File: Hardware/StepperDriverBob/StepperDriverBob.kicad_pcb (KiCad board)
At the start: 2 copper layers, 43.2 x 45.7 mm, 25 parts, among them J1 CONN_01X11, P1 CONN_01X02, P2 CONN_01X04, U1 DRV8825

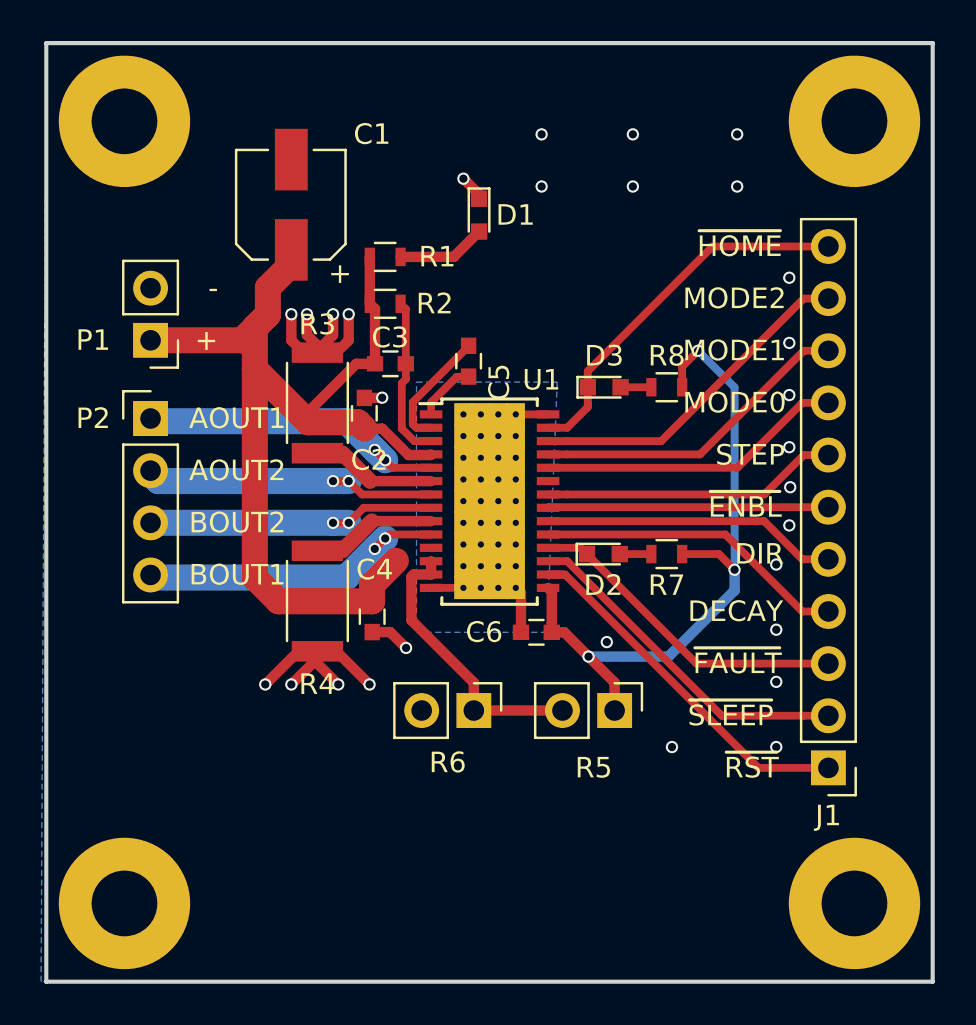
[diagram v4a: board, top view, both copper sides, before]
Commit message: Ordered Rev1
+added 2 100ohm resistor in place of 50 ohm
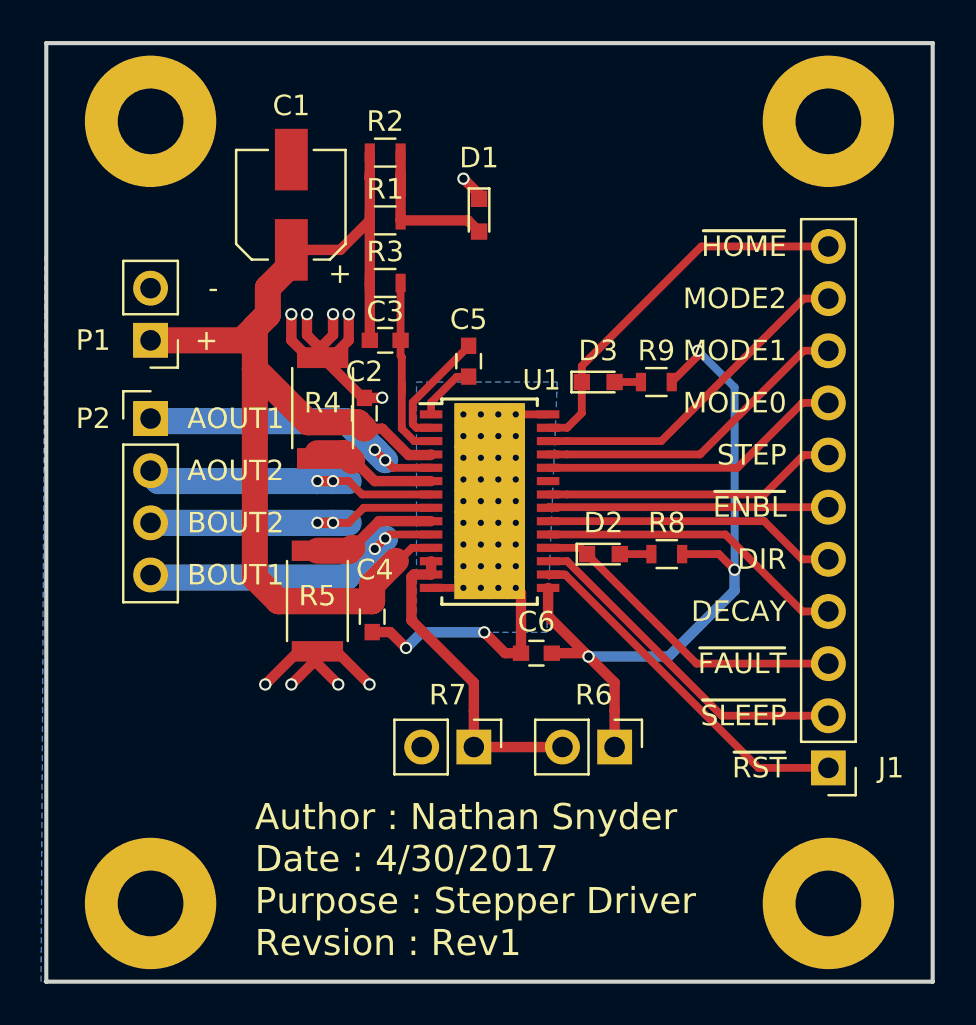
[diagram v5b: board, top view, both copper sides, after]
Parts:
- removed the ? at (128.3, 66.0)
- removed the ? at (163.8, 66.0)
- removed the ? at (163.8, 104.1)
- removed the ? at (128.3, 104.1)
- added ?: MOUNT1, Mounting_Holes:MountingHole_3.2mm_M3_Pad, F.Cu at (129.5, 66.0)
- added ?: MOUNT2, Mounting_Holes:MountingHole_3.2mm_M3_Pad, F.Cu at (162.6, 66.0)
- added ?: MOUNT3, Mounting_Holes:MountingHole_3.2mm_M3_Pad, F.Cu at (162.6, 104.1)
- added ?: MOUNT4, Mounting_Holes:MountingHole_3.2mm_M3_Pad, F.Cu at (129.5, 104.1)
- added R9: 100R, Resistors_SMD:R_0603, F.Cu at (154.2, 78.7)
- R1: value 50R -> 100R
- R2: value 1M -> 100R
- R3: value .2R -> 1M; footprint Resistors_SMD:R_2010 -> Resistors_SMD:R_0603
- R5: value 50k -> .2R; footprint Pin_Headers:Pin_Header_Straight_1x02_Pitch2.54mm -> Resistors_SMD:R_2010
- R7: value 100R -> 50k; footprint Resistors_SMD:R_0603 -> Pin_Headers:Pin_Header_Straight_1x02_Pitch2.54mm
- moved R5 15.4 mm to (137.7, 89.4), turned to 90 degrees
- moved R7 13.3 mm to (145.3, 96.5), turned to 270 degrees
- moved R4 9.40 mm to (137.9, 80.0), turned to 270 degrees
- moved R8 8.13 mm to (154.7, 87.1)
- moved R2 7.37 mm to (141.0, 67.6)
- moved R6 7.08 mm to (152.1, 96.5)
- moved R3 6.71 mm to (141.0, 73.9), turned to 180 degrees
- moved R1 1.78 mm to (141.0, 70.9)
- moved C3 1.17 mm to (141.0, 76.7)
- moved C6 1.02 mm to (148.3, 91.9)
- moved D3 0.39 mm to (151.3, 78.7)
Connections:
- R2 pad 1: Net-(C3-Pad1) -> Net-(D1-Pad2)
- R3 pad 1: GND -> Net-(C3-Pad1)
- R3 pad 2: Net-(R3-Pad2) -> VDD
- R5 pad 1: +3V3 -> GND
- R6 pad 1: Net-(R5-Pad2) -> +3V3
- R6 pad 2: GND -> Net-(R6-Pad2)
- R7 pad 1: +3V3 -> Net-(R6-Pad2)
- R7 pad 2: Net-(D2-Pad2) -> GND
- R8 pad 2: Net-(D3-Pad2) -> Net-(D2-Pad2)
- U1 pad 12: Net-(R5-Pad2) -> Net-(R6-Pad2)
- U1 pad 13: Net-(R5-Pad2) -> Net-(R6-Pad2)
- U1 pad 6: Net-(R3-Pad2) -> Net-(R4-Pad2)
- U1 pad 9: Net-(R4-Pad2) -> Net-(R5-Pad2)
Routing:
- net Net-(R6-Pad2): track 0.00 -> 15.7 mm
- net GND: track 30.7 -> 40.6 mm, vias 29 -> 12
- net Net-(R5-Pad2): track 13.9 -> 6.34 mm
- net VDD: track 52.3 -> 58.5 mm
- net Net-(R3-Pad2): track 6.10 -> 0.00 mm
- net Net-(D1-Pad2): track 4.33 -> 8.37 mm
- net +3V3: track 33.5 -> 36.7 mm
- net Net-(C3-Pad1): track 7.94 -> 9.24 mm
- net /BOUT2: track 14.8 -> 15.5 mm
- net /A0UT2: track 14.9 -> 15.6 mm
- net Net-(R4-Pad2): track 6.13 -> 6.64 mm
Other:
- board text added: "Author : Nathan Snyder Date : 4/30/2017 Purpose : Stepper Driver Revsion : Rev1"

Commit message: I'm not entirely sure
Idk
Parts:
- removed ?: MOUNT1, Mounting_Holes:MountingHole_3.2mm_M3_Pad
- removed ?: MOUNT2, Mounting_Holes:MountingHole_3.2mm_M3_Pad
- removed ?: MOUNT3, Mounting_Holes:MountingHole_3.2mm_M3_Pad
- removed ?: MOUNT4, Mounting_Holes:MountingHole_3.2mm_M3_Pad
- removed D2: ~FAULT~, LEDs:LED_0603
- removed D3: ~HOME~, LEDs:LED_0603
- removed R2: 100R, Resistors_SMD:R_0603
- added TP1: MOUNT1, Mounting_Holes:MountingHole_3.2mm_M3_Pad, F.Cu at (146.1, 118.1)
- added TP2: MOUNT2, Mounting_Holes:MountingHole_3.2mm_M3_Pad, F.Cu at (146.1, 118.1)
- added TP3: MOUNT3, Mounting_Holes:MountingHole_3.2mm_M3_Pad, F.Cu at (146.1, 118.1)
- added TP4: MOUNT4, Mounting_Holes:MountingHole_3.2mm_M3_Pad, F.Cu at (146.1, 118.1)
- C1: footprint Capacitors_SMD:CP_Elec_5x5.3 -> Capacitors_SMD:CP_Elec_10x10
- R1: value 100R -> 750R
- R8, R9: value 100R -> 10k
- moved C1 21.6 mm to (142.2, 49.3), turned to 0 degrees
- moved R1 8.87 mm to (149.6, 72.9)
- moved D1 8.38 mm to (153.7, 68.6)
- moved R8 5.43 mm to (153.7, 92.5), turned to 90 degrees
- moved R9 2.97 mm to (151.4, 79.8)
- moved R3 1.63 mm to (142.2, 74.9)
- moved C3 1.27 mm to (142.2, 76.7)
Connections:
- R8 pad 2: Net-(D2-Pad2) -> /~FAULT~
- R9 pad 2: Net-(D3-Pad2) -> /~HOME~
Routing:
- net +3V3: track 36.7 -> 25.8 mm, vias 3 -> 2
- net VDD: track 58.5 -> 67.1 mm, vias 0 -> 2
- net /~FAULT~: track 16.0 -> 21.8 mm, vias 0 -> 2
- net Net-(D1-Pad2): track 8.37 -> 5.33 mm
- net Net-(D2-Pad2): track 1.54 -> 0.00 mm
- net Net-(D3-Pad2): track 1.28 -> 0.00 mm
- net Net-(C3-Pad1): track 9.24 -> 8.26 mm
- net /~RST~: track 18.3 -> 17.6 mm
- net GND: track 40.6 -> 39.9 mm, vias 12 -> 10
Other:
- board text added: "Author : Nathan Snyder Date : 5/3/2017 Purpose : Stepper Driver Revsion : Rev2"
- board text added: "Make footprint for C1. It needs to be 10.3mm x 10.3mm. The current footprint I'm using is 10x10."
- board text removed: "Author : Nathan Snyder Date : 4/30/2017 Purpose : Stepper Driver Revsion : Rev1"
